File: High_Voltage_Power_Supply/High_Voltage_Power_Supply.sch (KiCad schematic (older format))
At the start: 96 parts, among them J1 Conn_01x02_Female, J2 Conn_01x02_Female, J3 Conn_01x02_Female, J4 Conn_01x12_Female, Q1 Q_NMOS_GDS, Q2 Q_NMOS_GDS, Q3 Q_NMOS_GDS, Q4 Q_NIGBT_GCE, U1 LT3751-TSSOP, U10 ADR3412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

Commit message: updated BOM
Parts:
- added D10, D11, D12, D13, D14, D15, D4, D5, D6, D7, D8, D9: CMZ5956B, Diode_SMD:D_SMA, symbol Device:D_Zener
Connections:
- net GND: now also D11.2 (A), D15.2 (A), D7.2 (A)
- net at C18.1, D2.1 (K), J3.2 (Pin_2)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: now also D12.1 (K), D4.1 (K), D8.1 (K)
- new net: D4.2 (A), D5.1 (K)
- new net: D5.2 (A), D6.1 (K)
- new net: D6.2 (A), D7.1 (K)
- new net: D8.2 (A), D9.1 (K)
- new net: D10.1 (K), D9.2 (A)
- new net: D10.2 (A), D11.1 (K)
- new net: D12.2 (A), D13.1 (K)
- new net: D13.2 (A), D14.1 (K)
- new net: D14.2 (A), D15.1 (K)
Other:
- moved on the sheet: C28, J3, J4, Q4, U4, U5, U6

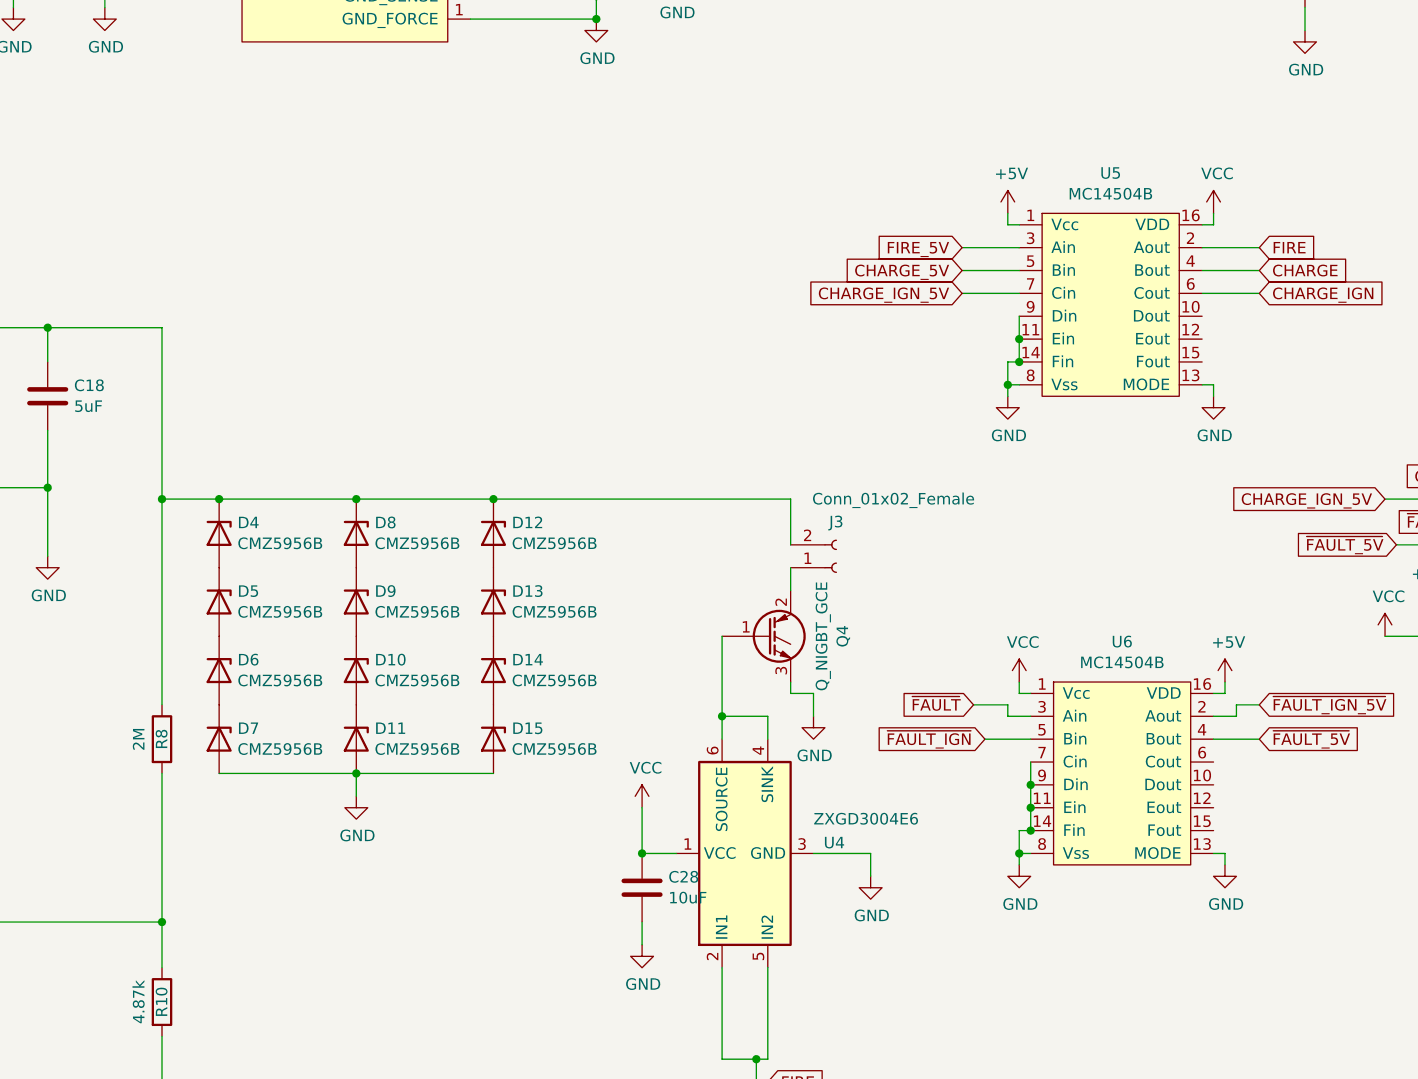
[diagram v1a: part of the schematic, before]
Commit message: routed most of the components on pcb
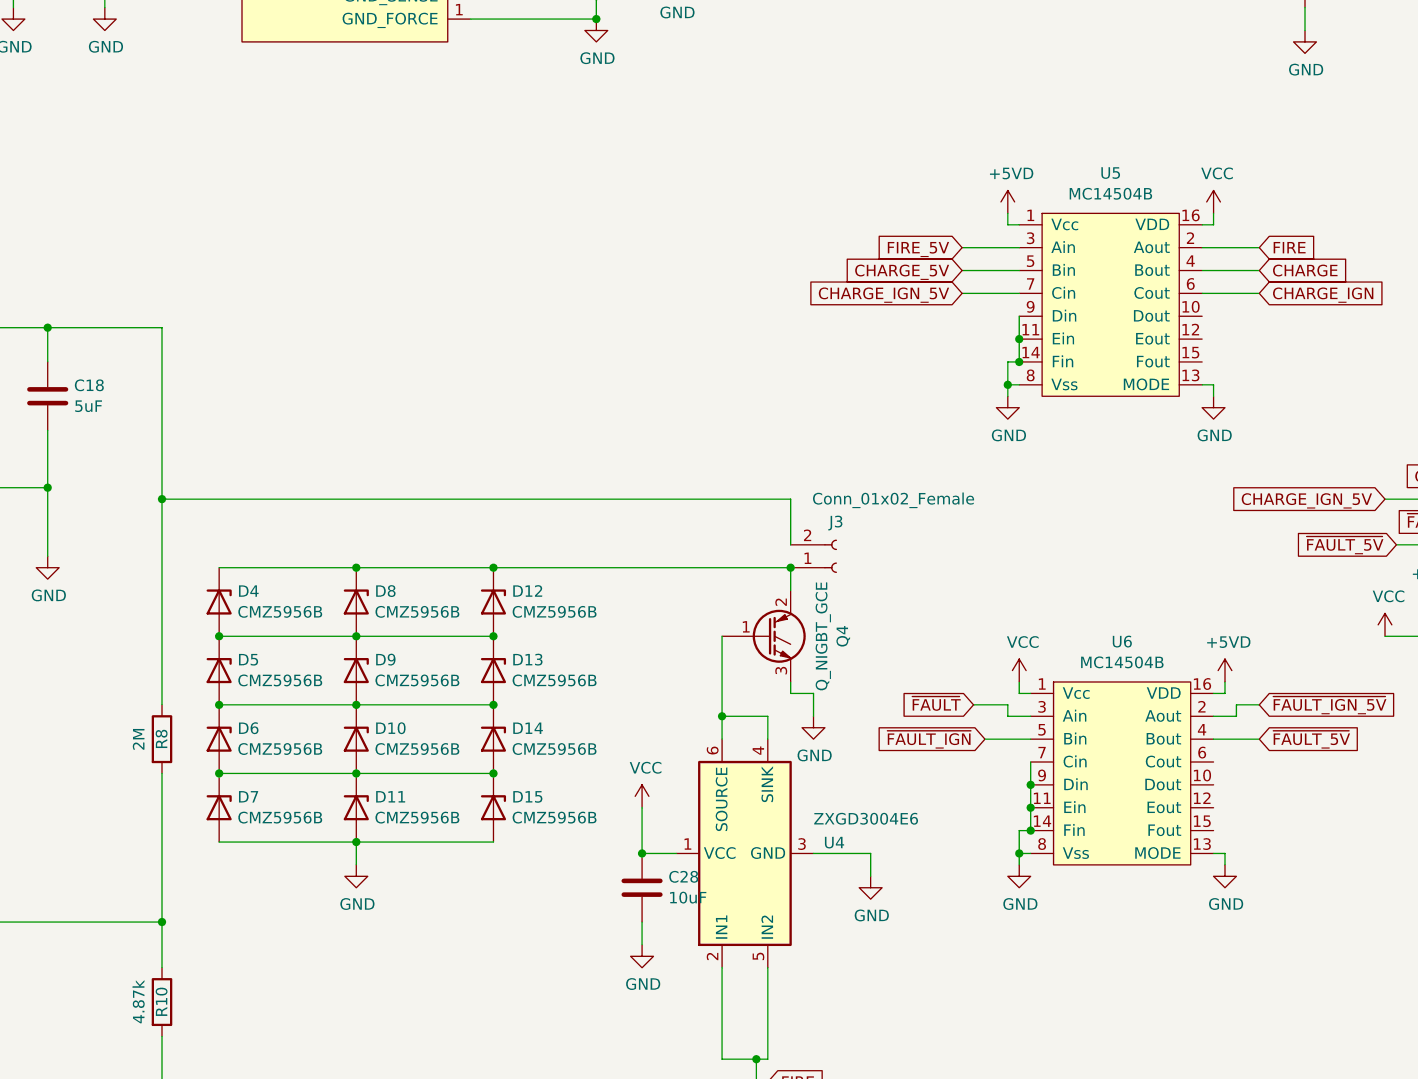
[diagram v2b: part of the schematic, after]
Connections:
- net +5V is gone; now on net +5VD: U5.1 (Vcc), U6.16 (VDD)
- net at C18.1, D2.1 (K), J3.2 (Pin_2)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: no longer D12.1 (K), D4.1 (K), D8.1 (K)
- net at J3.1 (Pin_1), Q4.2 (C): now also D12.1 (K), D4.1 (K), D8.1 (K)
- net at D4.2 (A), D5.1 (K): now also D12.2 (A), D13.1 (K), D8.2 (A), D9.1 (K)
- net at D5.2 (A), D6.1 (K): now also D10.1 (K), D13.2 (A), D14.1 (K), D9.2 (A)
- net at D6.2 (A), D7.1 (K): now also D10.2 (A), D11.1 (K), D14.2 (A), D15.1 (K)
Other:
- moved on the sheet: D10, D11, D12, D13, D14, D15, D4, D5, D6, D7, D8, D9
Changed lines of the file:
@@
-	1    0    0    -1
-$EndComp
-$Comp
-L power:+5V #PWR0139
-U 1 1 5FBA0E07
-P 12550 6300
-F 0 "#PWR0139" H 12550 6150 50  0001 C CNN
-F 1 "+5V" H 12565 6473 50  0000 C CNN
-F 2 "" H 12550 6300 50  0001 C CNN
-F 3 "" H 12550 6300 50  0001 C CNN
-	1    12550 6300
 	1    0    0    -1
 $EndComp
@@
 Wire Wire Line
 	12550 6350 12600 6350
-$Comp
-L power:+5V #PWR0140
-U 1 1 5FBAF7ED
-P 13500 8350
-F 0 "#PWR0140" H 13500 8200 50  0001 C CNN
-F 1 "+5V" H 13515 8523 50  0000 C CNN
-F 2 "" H 13500 8350 50  0001 C CNN
-F 3 "" H 13500 8350 50  0001 C CNN
-	1    13500 8350
-	1    0    0    -1
-$EndComp
 Wire Wire Line
 	13450 8400 13500 8400
@@
 L Device:D_Zener D4
 U 1 1 60EBCDC1
-P 9100 7700
-F 0 "D4" V 9054 7780 50  0000 L CNN
-F 1 "CMZ5956B" V 9145 7780 50  0000 L CNN
-F 2 "Diode_SMD:D_SMA" H 9100 7700 50  0001 C CNN
-F 3 "https://my.centralsemi.com/datasheets/CMZ5921B.PDF" H 9100 7700 50  0001 C CNN
-F 4 "https://www.digikey.com/en/products/detail/central-semiconductor-corp/CMZ5956B-TR13-PBFREE/5325082" H 9100 7700 50  0001 C CNN "Link"
-F 5 "200V" H 9100 7700 50  0001 C CNN "Voltage"
-	1    9100 7700
-	0    1    1    0
-$EndComp
-Wire Wire Line
-	8850 6800 8850 7550
-Connection ~ 8850 7550
-Wire Wire Line
-	8850 7550 8850 8450
-$Comp
-L Device:D_Zener D5
-U 1 1 60F50017
 P 9100 8000
-F 0 "D5" V 9054 8080 50  0000 L CNN
+F 0 "D4" V 9054 8080 50  0000 L CNN
 F 1 "CMZ5956B" V 9145 8080 50  0000 L CNN
 F 2 "Diode_SMD:D_SMA" H 9100 8000 50  0001 C CNN
@@
 	0    1    1    0
 $EndComp
-$Comp
-L Device:D_Zener D6
-U 1 1 60F506B5
+Wire Wire Line
+	8850 6800 8850 7550
+Connection ~ 8850 7550
+Wire Wire Line
+	8850 7550 8850 8450
+$Comp
+L Device:D_Zener D5
+U 1 1 60F50017
 P 9100 8300
-F 0 "D6" V 9054 8380 50  0000 L CNN
+F 0 "D5" V 9054 8380 50  0000 L CNN
 F 1 "CMZ5956B" V 9145 8380 50  0000 L CNN
 F 2 "Diode_SMD:D_SMA" H 9100 8300 50  0001 C CNN
@@
 $EndComp
 $Comp
-L Device:D_Zener D7
-U 1 1 60F50C84
+L Device:D_Zener D6
+U 1 1 60F506B5
 P 9100 8600
-F 0 "D7" V 9054 8680 50  0000 L CNN
+F 0 "D6" V 9054 8680 50  0000 L CNN
 F 1 "CMZ5956B" V 9145 8680 50  0000 L CNN
 F 2 "Diode_SMD:D_SMA" H 9100 8600 50  0001 C CNN
@@
 	0    1    1    0
 $EndComp
-Wire Wire Line
-	8850 7550 9100 7550
-Connection ~ 9100 7550
-Wire Wire Line
-	9100 7550 9700 7550
+$Comp
+L Device:D_Zener D7
+U 1 1 60F50C84
+P 9100 8900
+F 0 "D7" V 9054 8980 50  0000 L CNN
+F 1 "CMZ5956B" V 9145 8980 50  0000 L CNN
+F 2 "Diode_SMD:D_SMA" H 9100 8900 50  0001 C CNN
+F 3 "https://my.centralsemi.com/datasheets/CMZ5921B.PDF" H 9100 8900 50  0001 C CNN
+F 4 "https://www.digikey.com/en/products/detail/central-semiconductor-corp/CMZ5956B-TR13-PBFREE/5325082" H 9100 8900 50  0001 C CNN "Link"
+F 5 "200V" H 9100 8900 50  0001 C CNN "Voltage"
+	1    9100 8900
+	0    1    1    0
+$EndComp
 $Comp
 L Device:D_Zener D8
 U 1 1 6103547D
-P 9700 7700
-F 0 "D8" V 9654 7780 50  0000 L CNN
-F 1 "CMZ5956B" V 9745 7780 50  0000 L CNN
-F 2 "Diode_SMD:D_SMA" H 9700 7700 50  0001 C CNN
-F 3 "https://my.centralsemi.com/datasheets/CMZ5921B.PDF" H 9700 7700 50  0001 C CNN
-F 4 "https://www.digikey.com/en/products/detail/central-semiconductor-corp/CMZ5956B-TR13-PBFREE/5325082" H 9700 7700 50  0001 C CNN "Link"
-F 5 "200V" H 9700 7700 50  0001 C CNN "Voltage"
-	1    9700 7700
-	0    1    1    0
-$EndComp
-$Comp
-L Device:D_Zener D9
-U 1 1 61035483
 P 9700 8000
-F 0 "D9" V 9654 8080 50  0000 L CNN
+F 0 "D8" V 9654 8080 50  0000 L CNN
 F 1 "CMZ5956B" V 9745 8080 50  0000 L CNN
 F 2 "Diode_SMD:D_SMA" H 9700 8000 50  0001 C CNN
@@
 $EndComp
 $Comp
-L Device:D_Zener D10
-U 1 1 61035489
+L Device:D_Zener D9
+U 1 1 61035483
 P 9700 8300
-F 0 "D10" V 9654 8380 50  0000 L CNN
+F 0 "D9" V 9654 8380 50  0000 L CNN
 F 1 "CMZ5956B" V 9745 8380 50  0000 L CNN
 F 2 "Diode_SMD:D_SMA" H 9700 8300 50  0001 C CNN
@@
 $EndComp
 $Comp
-L Device:D_Zener D11
-U 1 1 6103548F
+L Device:D_Zener D10
+U 1 1 61035489
 P 9700 8600
-F 0 "D11" V 9654 8680 50  0000 L CNN
+F 0 "D10" V 9654 8680 50  0000 L CNN
 F 1 "CMZ5956B" V 9745 8680 50  0000 L CNN
 F 2 "Diode_SMD:D_SMA" H 9700 8600 50  0001 C CNN
@@
 $EndComp
 $Comp
+L Device:D_Zener D11
+U 1 1 6103548F
+P 9700 8900
+F 0 "D11" V 9654 8980 50  0000 L CNN
+F 1 "CMZ5956B" V 9745 8980 50  0000 L CNN
+F 2 "Diode_SMD:D_SMA" H 9700 8900 50  0001 C CNN
+F 3 "https://my.centralsemi.com/datasheets/CMZ5921B.PDF" H 9700 8900 50  0001 C CNN
+F 4 "https://www.digikey.com/en/products/detail/central-semiconductor-corp/CMZ5956B-TR13-PBFREE/5325082" H 9700 8900 50  0001 C CNN "Link"
+F 5 "200V" H 9700 8900 50  0001 C CNN "Voltage"
+	1    9700 8900
+	0    1    1    0
+$EndComp
+$Comp
 L Device:D_Zener D12
 U 1 1 61053F69
-P 10300 7700
-F 0 "D12" V 10254 7780 50  0000 L CNN
-F 1 "CMZ5956B" V 10345 7780 50  0000 L CNN
-F 2 "Diode_SMD:D_SMA" H 10300 7700 50  0001 C CNN
-F 3 "https://my.centralsemi.com/datasheets/CMZ5921B.PDF" H 10300 7700 50  0001 C CNN
-F 4 "https://www.digikey.com/en/products/detail/central-semiconductor-corp/CMZ5956B-TR13-PBFREE/5325082" H 10300 7700 50  0001 C CNN "Link"
-F 5 "200V" H 10300 7700 50  0001 C CNN "Voltage"
-	1    10300 7700
-	0    1    1    0
-$EndComp
-$Comp
-L Device:D_Zener D13
-U 1 1 61053F6F
 P 10300 8000
-F 0 "D13" V 10254 8080 50  0000 L CNN
+F 0 "D12" V 10254 8080 50  0000 L CNN
 F 1 "CMZ5956B" V 10345 8080 50  0000 L CNN
 F 2 "Diode_SMD:D_SMA" H 10300 8000 50  0001 C CNN
@@
 $EndComp
 $Comp
-L Device:D_Zener D14
-U 1 1 61053F75
+L Device:D_Zener D13
+U 1 1 61053F6F
 P 10300 8300
-F 0 "D14" V 10254 8380 50  0000 L CNN
+F 0 "D13" V 10254 8380 50  0000 L CNN
 F 1 "CMZ5956B" V 10345 8380 50  0000 L CNN
 F 2 "Diode_SMD:D_SMA" H 10300 8300 50  0001 C CNN
@@
 $EndComp
 $Comp
-L Device:D_Zener D15
-U 1 1 61053F7B
+L Device:D_Zener D14
+U 1 1 61053F75
 P 10300 8600
-F 0 "D15" V 10254 8680 50  0000 L CNN
+F 0 "D14" V 10254 8680 50  0000 L CNN
 F 1 "CMZ5956B" V 10345 8680 50  0000 L CNN
 F 2 "Diode_SMD:D_SMA" H 10300 8600 50  0001 C CNN
@@
 	0    1    1    0
 $EndComp
-Connection ~ 9700 7550
-Wire Wire Line
-	9700 7550 10300 7550
-Connection ~ 10300 7550
-Wire Wire Line
-	10300 7550 11600 7550
-Wire Wire Line
-	9100 8750 9700 8750
-Connection ~ 9700 8750
-Wire Wire Line
-	9700 8750 10300 8750
+$Comp
+L Device:D_Zener D15
+U 1 1 61053F7B
+P 10300 8900
+F 0 "D15" V 10254 8980 50  0000 L CNN
+F 1 "CMZ5956B" V 10345 8980 50  0000 L CNN
+F 2 "Diode_SMD:D_SMA" H 10300 8900 50  0001 C CNN
+F 3 "https://my.centralsemi.com/datasheets/CMZ5921B.PDF" H 10300 8900 50  0001 C CNN
+F 4 "https://www.digikey.com/en/products/detail/central-semiconductor-corp/CMZ5956B-TR13-PBFREE/5325082" H 10300 8900 50  0001 C CNN "Link"
+F 5 "200V" H 10300 8900 50  0001 C CNN "Voltage"
+	1    10300 8900
+	0    1    1    0
+$EndComp
+Wire Wire Line
+	9100 9050 9700 9050
+Connection ~ 9700 9050
+Wire Wire Line
+	9700 9050 10300 9050
 $Comp
 L power:GND #PWR01
 U 1 1 610CFFA9
-P 9700 8850
-F 0 "#PWR01" H 9700 8600 50  0001 C CNN
-F 1 "GND" H 9705 8677 50  0000 C CNN
-F 2 "" H 9700 8850 50  0001 C CNN
-F 3 "" H 9700 8850 50  0001 C CNN
-	1    9700 8850
-	1    0    0    -1
-$EndComp
-Wire Wire Line
-	9700 8850 9700 8750
+P 9700 9150
+F 0 "#PWR01" H 9700 8900 50  0001 C CNN
+F 1 "GND" H 9705 8977 50  0000 C CNN
+F 2 "" H 9700 9150 50  0001 C CNN
+F 3 "" H 9700 9150 50  0001 C CNN
+	1    9700 9150
+	1    0    0    -1
+$EndComp
+Wire Wire Line
+	9700 9150 9700 9050
+Wire Wire Line
+	8850 7550 11600 7550
+Wire Wire Line
+	11600 7850 10300 7850
+Connection ~ 11600 7850
+Connection ~ 9700 7850
+Wire Wire Line
+	9700 7850 9100 7850
+Connection ~ 10300 7850
+Wire Wire Line
+	10300 7850 9700 7850
+Wire Wire Line
+	10300 8150 9700 8150
+Connection ~ 10300 8150
+Connection ~ 9100 8150
+Connection ~ 9700 8150
+Wire Wire Line
+	9700 8150 9100 8150
+Wire Wire Line
+	9100 8450 9700 8450
+Connection ~ 9100 8450
+Connection ~ 10300 8450
+Connection ~ 9700 8450
+Wire Wire Line
+	9700 8450 10300 8450
+Wire Wire Line
+	10300 8750 9700 8750
+Connection ~ 10300 8750
+Connection ~ 9100 8750
+Connection ~ 9700 8750
+Wire Wire Line
+	9700 8750 9100 8750
+$Comp
+L power:+5VD #PWR?
+U 1 1 6123F13A
+P 13500 8350
+F 0 "#PWR?" H 13500 8200 50  0001 C CNN
+F 1 "+5VD" H 13515 8523 50  0000 C CNN
+F 2 "" H 13500 8350 50  0001 C CNN
+F 3 "" H 13500 8350 50  0001 C CNN
+	1    13500 8350
+	1    0    0    -1
+$EndComp
+$Comp
+L power:+5VD #PWR?
+U 1 1 612430CA
+P 12550 6300
+F 0 "#PWR?" H 12550 6150 50  0001 C CNN
+F 1 "+5VD" H 12565 6473 50  0000 C CNN
+F 2 "" H 12550 6300 50  0001 C CNN
+F 3 "" H 12550 6300 50  0001 C CNN
+	1    12550 6300
+	1    0    0    -1
+$EndComp
 $EndSCHEMATC
